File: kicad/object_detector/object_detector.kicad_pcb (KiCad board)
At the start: 2 copper layers, 85.5 x 75.5 mm, 16 parts, among them U1 LM386

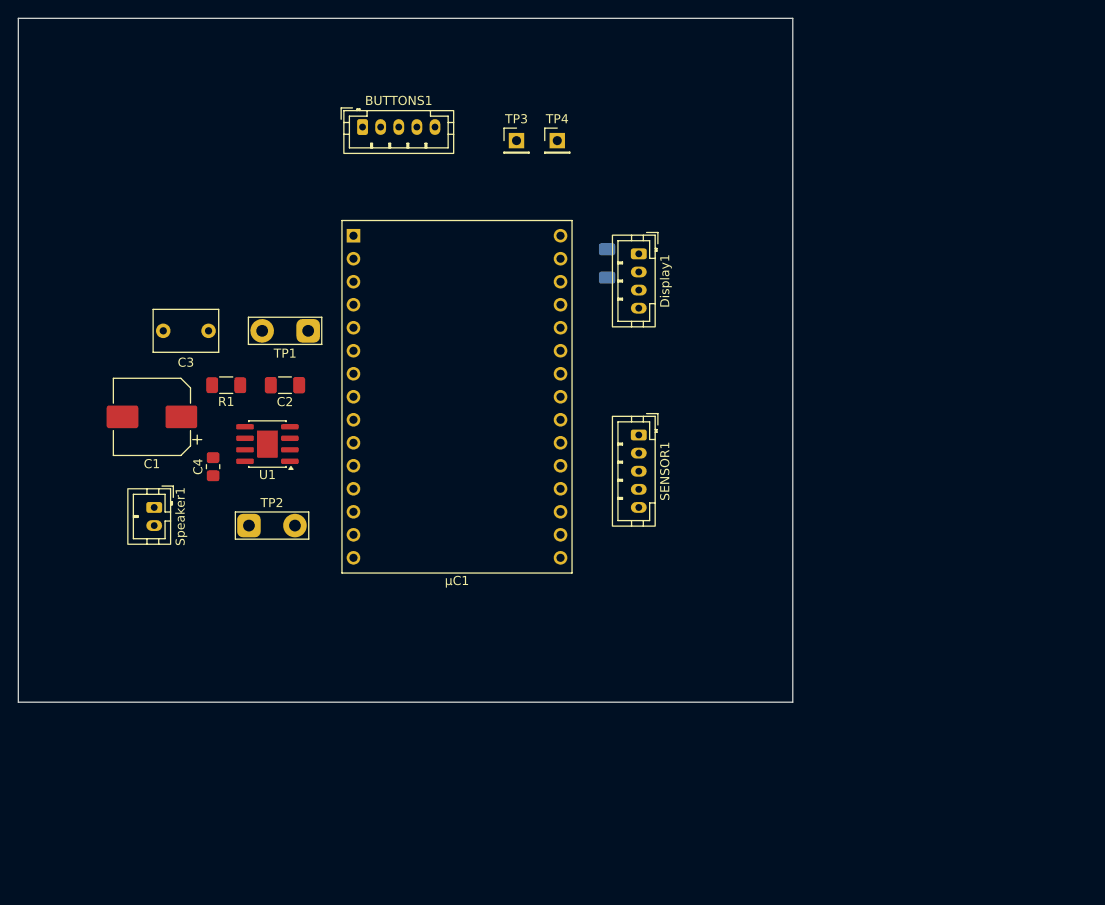
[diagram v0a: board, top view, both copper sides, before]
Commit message: preliminary layout
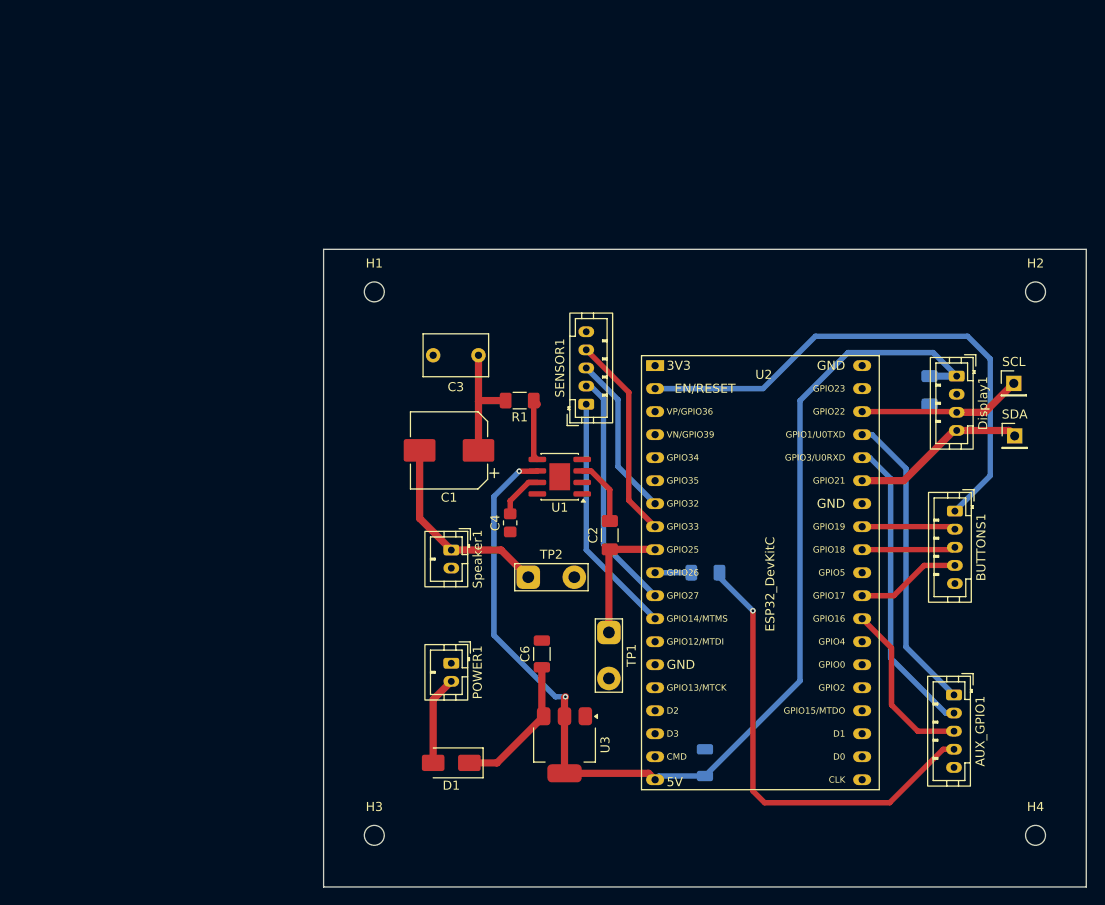
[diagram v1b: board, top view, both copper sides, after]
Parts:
- removed µC1: ~, RF_Module:ESP32-C3-DevKitM-1
- added AUX_GPIO1: Conn_01x05, Connector_JST:JST_PH_B5B-PH-K_1x05_P2.00mm_Vertical, F.Cu at (170.8, 108.7)
- added C6: 10uF, Capacitor_SMD:C_1206_3216Metric, F.Cu at (125.3, 104.2)
- added C7: 10uF, Capacitor_SMD:C_1206_3216Metric, B.Cu at (143.3, 116.2)
- added D1: B220, Diode_SMD:D_SMA, F.Cu at (115.3, 116.2)
- added H1: MountingHole, MountingHole:MountingHole_2.2mm_M2, F.Cu at (106.8, 64.2)
- added H2: MountingHole, MountingHole:MountingHole_2.2mm_M2, F.Cu at (179.8, 64.2)
- added H3: MountingHole, MountingHole:MountingHole_2.2mm_M2, F.Cu at (106.8, 124.2)
- added H4: MountingHole, MountingHole:MountingHole_2.2mm_M2, F.Cu at (179.8, 124.2)
- added POWER1: Conn_01x02, Connector_JST:JST_PH_B2B-PH-K_1x02_P2.00mm_Vertical, F.Cu at (115.3, 105.2)
- added R2: 0R, Resistor_SMD:R_1206_3216Metric_Pad1.30x1.75mm_HandSolder, B.Cu at (143.3, 95.2)
- added U2: ESP32_DevKitC, PCM_Espressif:ESP32-DevKitC, F.Cu at (137.8, 72.3)
- added U3: NCP1117-5.0_SOT223, Package_TO_SOT_SMD:SOT-223-3_TabPin2, F.Cu at (127.8, 114.2)
- moved BUTTONS1 77.9 mm to (170.9, 88.4), turned to -90 degrees
- moved SCL 61.1 mm to (177.4, 74.3)
- moved SDA 60.1 mm to (177.5, 80.1)
- moved TP1 47.0 mm to (132.7, 101.8), turned to -90 degrees
- moved C2 39.5 mm to (132.8, 91.1), turned to 90 degrees
- moved C5 38.3 mm to (168.1, 75.1)
- moved Display1 37.6 mm to (171.1, 73.5)
- moved C4 33.4 mm to (121.8, 89.7)
- moved Speaker1 33.1 mm to (115.3, 92.7)
- moved C1 33.0 mm to (115.0, 81.7)
- moved U1 32.5 mm to (127.3, 84.6)
- moved R1 32.4 mm to (122.8, 76.2)
- moved TP2 31.4 mm to (123.8, 95.7)
- moved C3 29.9 mm to (118.3, 71.2)
- moved SENSOR1 6.72 mm to (130.2, 76.6), turned to 90 degrees
- renumbered TP3 to SCL, TP4 to SDA
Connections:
- net /SCL renamed SCL
- net /SDA renamed SDA
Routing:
- net 5V: track 0.00 -> 126.1 mm, vias 0 -> 2
- net RESET: track 0.00 -> 58.8 mm
- net Net-(AUX_GPIO1-Pin_4): track 0.00 -> 50.8 mm, vias 0 -> 1
- net TX: track 0.00 -> 33.6 mm
- net RX: track 0.00 -> 33.4 mm
- net WEIGH_1: track 0.00 -> 26.8 mm
- net WEIGH_2: track 0.00 -> 26.6 mm
- net WEIGH_4: track 0.00 -> 22.7 mm
- net Net-(Speaker1-Pin_1): track 0.00 -> 22.2 mm
- net SDA: track 0.00 -> 19.4 mm
- net GPIO_16: track 0.00 -> 19.0 mm
- net WEIGH_3: track 0.00 -> 18.1 mm
- net SCL: track 0.00 -> 18.1 mm
- net Net-(D1-K): track 0.00 -> 15.8 mm
- net Net-(C1-Pad1): track 0.00 -> 14.4 mm
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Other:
- board size 85.5 x 75.5 mm -> 84.2 x 70.4 mm

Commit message: added dimensions to PCB footprint
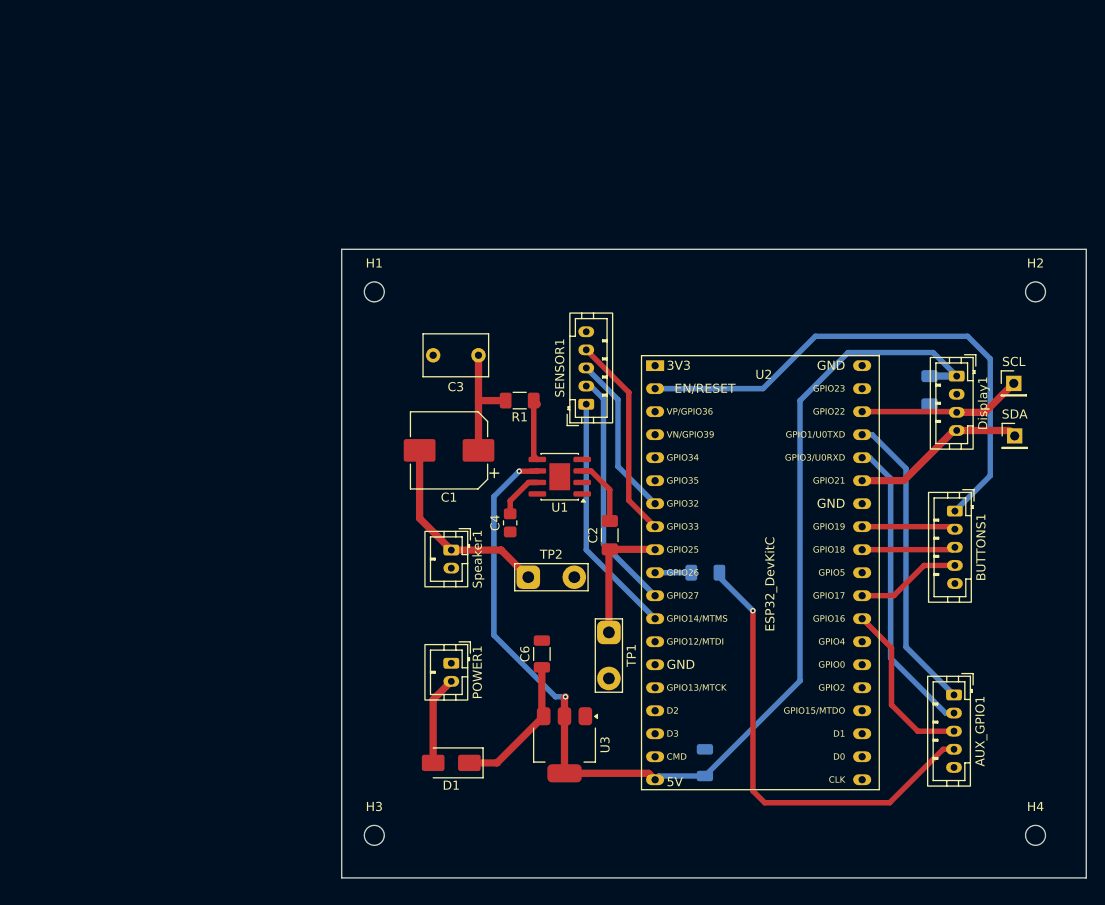
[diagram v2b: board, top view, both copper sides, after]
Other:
- board size 84.2 x 70.4 mm -> 82.2 x 69.4 mm
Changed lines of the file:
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@@
 			)
 		)
-		(fp_text user "GND"
-			(at 21 15.24 0)
-			(unlocked yes)
-			(layer "F.SilkS")
-			(effects
-				(font
-					(size 1 1)
-					(thickness 0.15)
-				)
-				(justify right)
-			)
-		)
 		(fp_text user "GPIO25"
 			(at 1.27 20.32 0)
@@
 			)
 		)
+		(fp_text user "GND"
+			(at 21 15.24 0)
+			(unlocked yes)
+			(layer "F.SilkS")
+			(effects
+				(font
+					(size 1 1)
+					(thickness 0.15)
+				)
+				(justify right)
+			)
+		)
 		(fp_text user "GPIO19"
 			(at 21 17.78 0)
@@
 	)
 	(gr_rect
-		(start 101.2 59.5)
-		(end 185.4 129.9)
+		(start 103.2 59.5)
+		(end 185.4 128.9)
 		(stroke
 			(width 0.05)
@@
 		(layer "Edge.Cuts")
 	)
+	(dimension
+		(type orthogonal)
+		(layer "F.Cu")
+		(pts
+			(xy 185.4 59.5) (xy 103.2 59.5)
+		)
+		(height -2.5)
+		(orientation 0)
+		(format
+			(prefix "")
+			(suffix "")
+			(units 3)
+			(units_format 0)
+			(precision 4)
+			(suppress_zeroes yes)
+		)
+		(style
+			(thickness 0.2)
+			(arrow_length 1.27)
+			(text_position_mode 0)
+			(arrow_direction outward)
+			(extension_height 0.58642)
+			(extension_offset 0.5)
+			(keep_text_aligned yes)
+		)
+		(gr_text "82.2"
+			(at 144.3 55.2 0)
+			(layer "F.Cu")
+			(effects
+				(font
+					(size 1.5 1.5)
+					(thickness 0.3)
+				)
+			)
+		)
+	)
+	(dimension
+		(type orthogonal)
+		(layer "F.Cu")
+		(pts
+			(xy 103.2 59.5) (xy 103.2 128.9)
+		)
+		(height -4.2)
+		(orientation 1)
+		(format
+			(prefix "")
+			(suffix "")
+			(units 3)
+			(units_format 0)
+			(precision 4)
+			(suppress_zeroes yes)
+		)
+		(style
+			(thickness 0.2)
+			(arrow_length 1.27)
+			(text_position_mode 0)
+			(arrow_direction outward)
+			(extension_height 0.58642)
+			(extension_offset 0.5)
+			(keep_text_aligned yes)
+		)
+		(gr_text "69.4"
+			(at 97.2 94.2 90)
+			(layer "F.Cu")
+			(effects
+				(font
+					(size 1.5 1.5)
+					(thickness 0.3)
+				)
+			)
+		)
+	)
 	(segment

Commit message: PCB edits, MC code edits
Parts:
- added G***: LOGO, Graphics:Abbey image, B.Cu at (153.7, 79.6)
- moved SCL 11.2 mm to (174.0, 85.0)
- moved SDA 9.81 mm to (169.0, 85.0)
- moved H3 7.88 mm to (114.0, 121.0)
- moved H1 7.73 mm to (114.0, 67.0)
- moved H4 6.62 mm to (174.0, 121.0)
- moved H2 6.44 mm to (174.0, 67.0)
- moved D1 4.89 mm to (119.0, 113.0)
- moved C5 4.10 mm to (164.0, 75.0)
- moved POWER1 3.48 mm to (118.0, 103.0)
- moved AUX_GPIO1 3.24 mm to (169.0, 106.0)
- moved BUTTONS1 3.22 mm to (169.0, 91.0)
- moved Speaker1 2.79 mm to (118.0, 92.0)
- moved Display1 2.16 mm to (169.0, 73.0)
- moved C1 1.95 mm to (117.0, 81.7)
- moved C6 1.37 mm to (126.0, 103.0)
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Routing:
- net GND: track 0.00 -> 19.0 mm, vias 0 -> 5
- net GPIO_16: track 19.0 -> 13.8 mm
- net SDA: track 19.4 -> 14.8 mm
- net RX: track 33.4 -> 29.5 mm
- net TX: track 33.6 -> 30.1 mm
- net TIME_DEC: track 11.6 -> 8.65 mm
- net 5V: track 126.1 -> 123.1 mm
- net Net-(D1-K): track 15.8 -> 13.1 mm
- net Net-(U1-+): track 7.36 -> 8.88 mm
- net Net-(D1-A): track 9.83 -> 8.41 mm
- net Net-(Speaker1-Pin_1): track 22.2 -> 20.8 mm
- net SCL: track 18.1 -> 19.2 mm
- net TIME_INC: track 10.3 -> 9.31 mm
- net BRIGHTNESS: track 10.4 -> 9.53 mm
- added copper zone on B.Cu, net GND
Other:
- board size 82.2 x 69.4 mm -> 66 x 60 mm
- rule pad_to_mask_clearance: 0 -> 0.0508
- board text added: "5V"
- board text added: "Brightn"
- board text added: "GND"
- board text added: "IO_16"
- board text added: "IO_26"
- board text added: "Nicholas Gerbavac John Ramus Arthur Roth"
- board text added: "OBJECT DETECTOR ECE342"
- board text added: "RX"
- board text added: "Reset"
- board text added: "SCL"
- board text added: "SDA"
- board text added: "TX"
- board text added: "T_Dec"
- board text added: "T_Inc"
- board text added: "W1"
- board text added: "W2"
- board text added: "W3"
- board text added: "W4"

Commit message: board revision friday
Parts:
- AUX GPIO: renamed from AUX_GPIO1
- C4: footprint Resistor_SMD:R_0805_2012Metric_Pad1.20x1.40mm_HandSolder -> Capacitor_SMD:C_1206_3216Metric_Pad1.33x1.80mm_HandSolder
- moved C6 15.1 mm to (118.7, 116.2), turned to 180 degrees
- moved C7 4.01 mm to (140.7, 119.2), turned to -90 degrees
- moved R1 3.45 mm to (124.7, 77.7), turned to 90 degrees
- moved C4 3.23 mm to (126.1, 90.9), turned to 180 degrees
- moved DAC 3.11 mm to (130.4, 103.9), turned to 180 degrees
- moved SPK 2.88 mm to (125.2, 98.2)
- moved D1 2.25 mm to (118.2, 110.9)
- moved R2 1.50 mm to (141.8, 95.2)
- moved C2 1.40 mm to (132.6, 91.1)
- renumbered BUTTONS1 to BUTTONS, TP1 to DAC, Display1 to DISPLAY, SENSOR1 to SENSOR, TP2 to SPK, Speaker1 to Speaker, POWER1 to 󰂅
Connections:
- Speaker pad 1: Net-(Speaker1-Pin_1) -> GND
- Speaker pad 2: GND -> Net-(Speaker1-Pin_1)
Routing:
- net GND: track 19.0 -> 3.14 mm, vias 5 -> 0
- net Net-(U1-BYPASS): track 5.08 -> 10.1 mm
- net DAC: track 14.2 -> 19.2 mm
- net Net-(C1-Pad1): track 14.7 -> 19.5 mm
- net Net-(R1-Pad1): track 7.72 -> 3.54 mm
- net Net-(Speaker1-Pin_1): track 20.8 -> 24.3 mm
- net WEIGH_1: track 26.8 -> 29.2 mm
- net Net-(D1-K): track 13.1 -> 11.0 mm
- net Net-(D1-A): track 8.41 -> 6.65 mm
- net EXT_DAC: track 4.00 -> 2.50 mm
- net Net-(AUX_GPIO1-Pin_4): track 51.3 -> 52.5 mm
- net WEIGH_3: track 18.1 -> 18.9 mm
- net GPIO_16: track 13.8 -> 14.4 mm
- net WEIGH_2: track 26.6 -> 27.1 mm
- added copper zone on F.Cu, net GND
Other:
- board text added: "Bright"
- board text added: "Time+"
- board text added: "Time-"
- board text added: ""
- board text added: "  "
- board text removed: "Brightn"
- board text removed: "T_Dec"
- board text removed: "T_Inc"

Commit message: final stuff on the pcb that i forgot to commit
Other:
- rule pad_to_mask_clearance: 0.0508 -> 0
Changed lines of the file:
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@@
 			(dielectric_constraints no)
 		)
-		(pad_to_mask_clearance 0.0508)
+		(pad_to_mask_clearance 0)
 		(allow_soldermask_bridges_in_footprints no)
 		(tenting front back)
 		(pcbplotparams
-			(layerselection 0x00000000_00000000_55555555_5755f5ff)
+			(layerselection 0x00000000_00000000_55555555_575555ff)
 			(plot_on_all_layers_selection 0x00000000_00000000_00000000_00000000)
 			(disableapertmacros no)
-			(usegerberextensions no)
+			(usegerberextensions yes)
 			(usegerberattributes yes)
 			(usegerberadvancedattributes yes)
@@
 			(outputformat 1)
 			(mirror no)
-			(drillshape 1)
+			(drillshape 0)
 			(scaleselection 1)
-			(outputdirectory "")
+			(outputdirectory "gerber/")
 		)
 	)
